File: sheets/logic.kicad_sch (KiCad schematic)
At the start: 25 parts, among them J6 MicroFit3.0_1x2, J7 MoRex_MicroFit-3.0_4x1, SW1 SW_Omron_B3FS, U5 ESP32-S3-DevKitC, U6 NRF24L01_Breakout, U7 PCA9685PW, U8 TCA9545APWR, U9 BTT_TMC2209

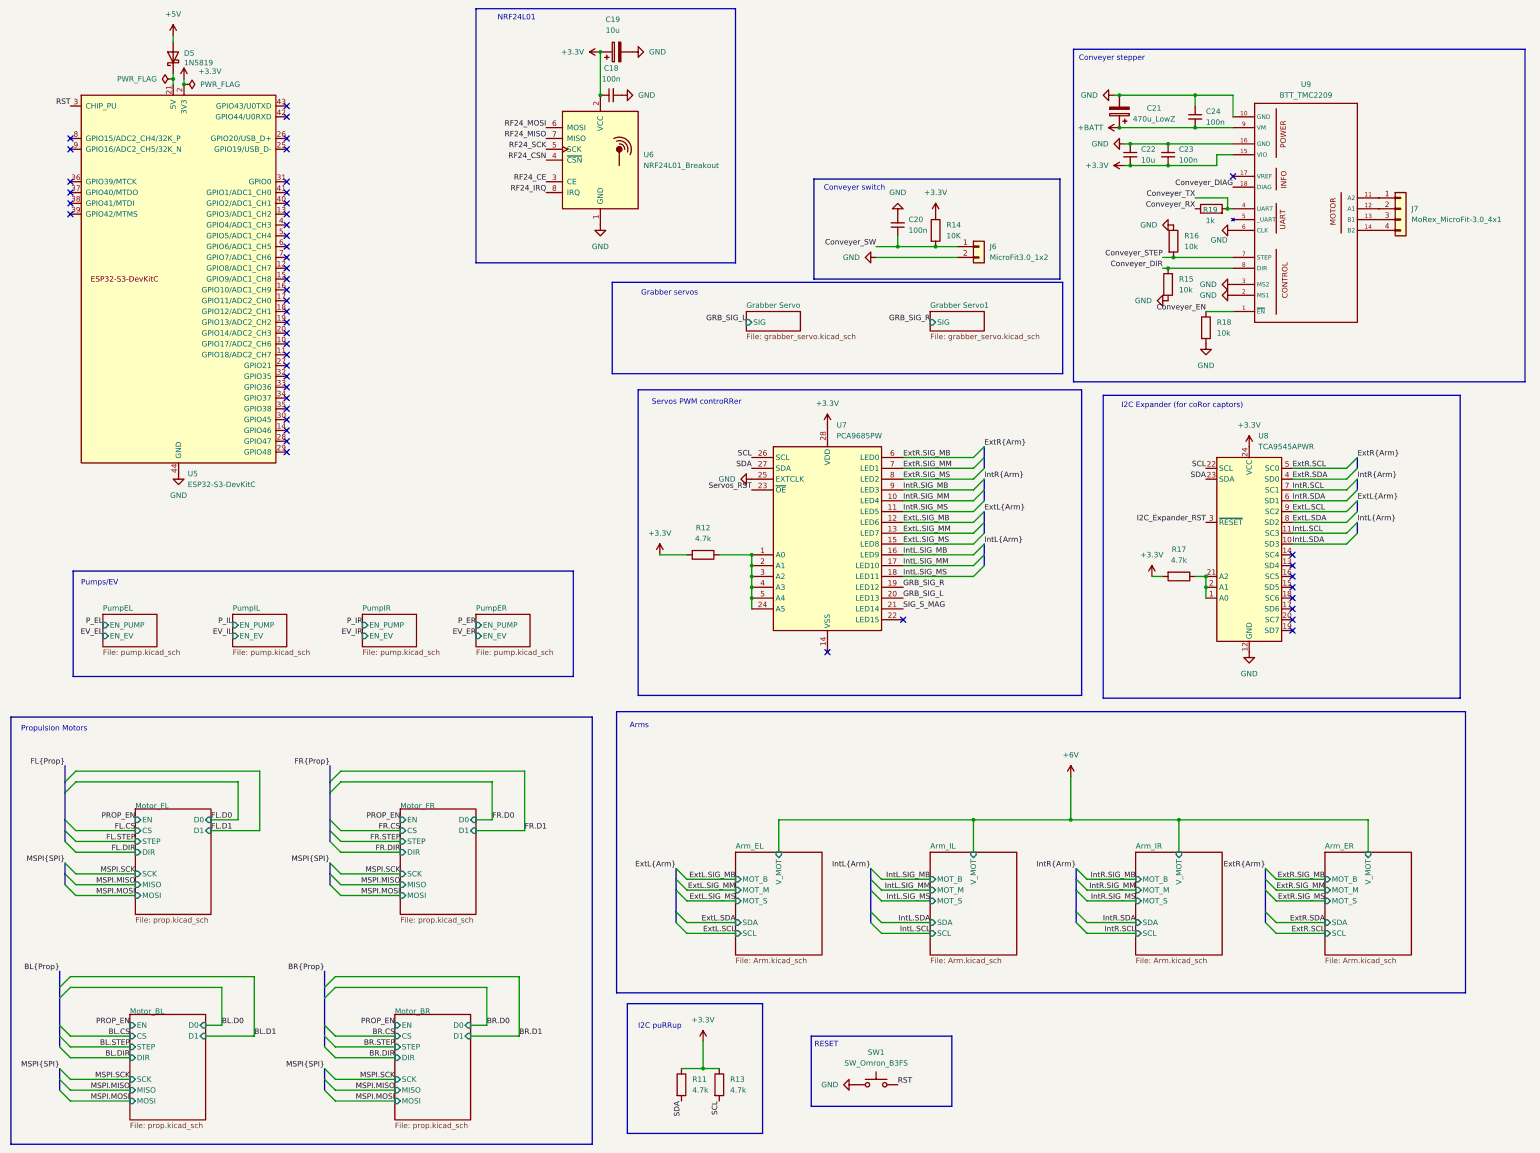
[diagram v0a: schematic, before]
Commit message: Add CB1-P-12V relay footprint, 3D model, and symbols
Added CB1-P-12V.stp 3D model and CB1P12V.kicad_mod footprint to the libs directory. Updated libs/sym.kicad_sym and multiple schematic sheets to include and reference the new relay. Adjusted eurobot-2026-robot-pcb.kicad_pro BOM and group settings to support new components.
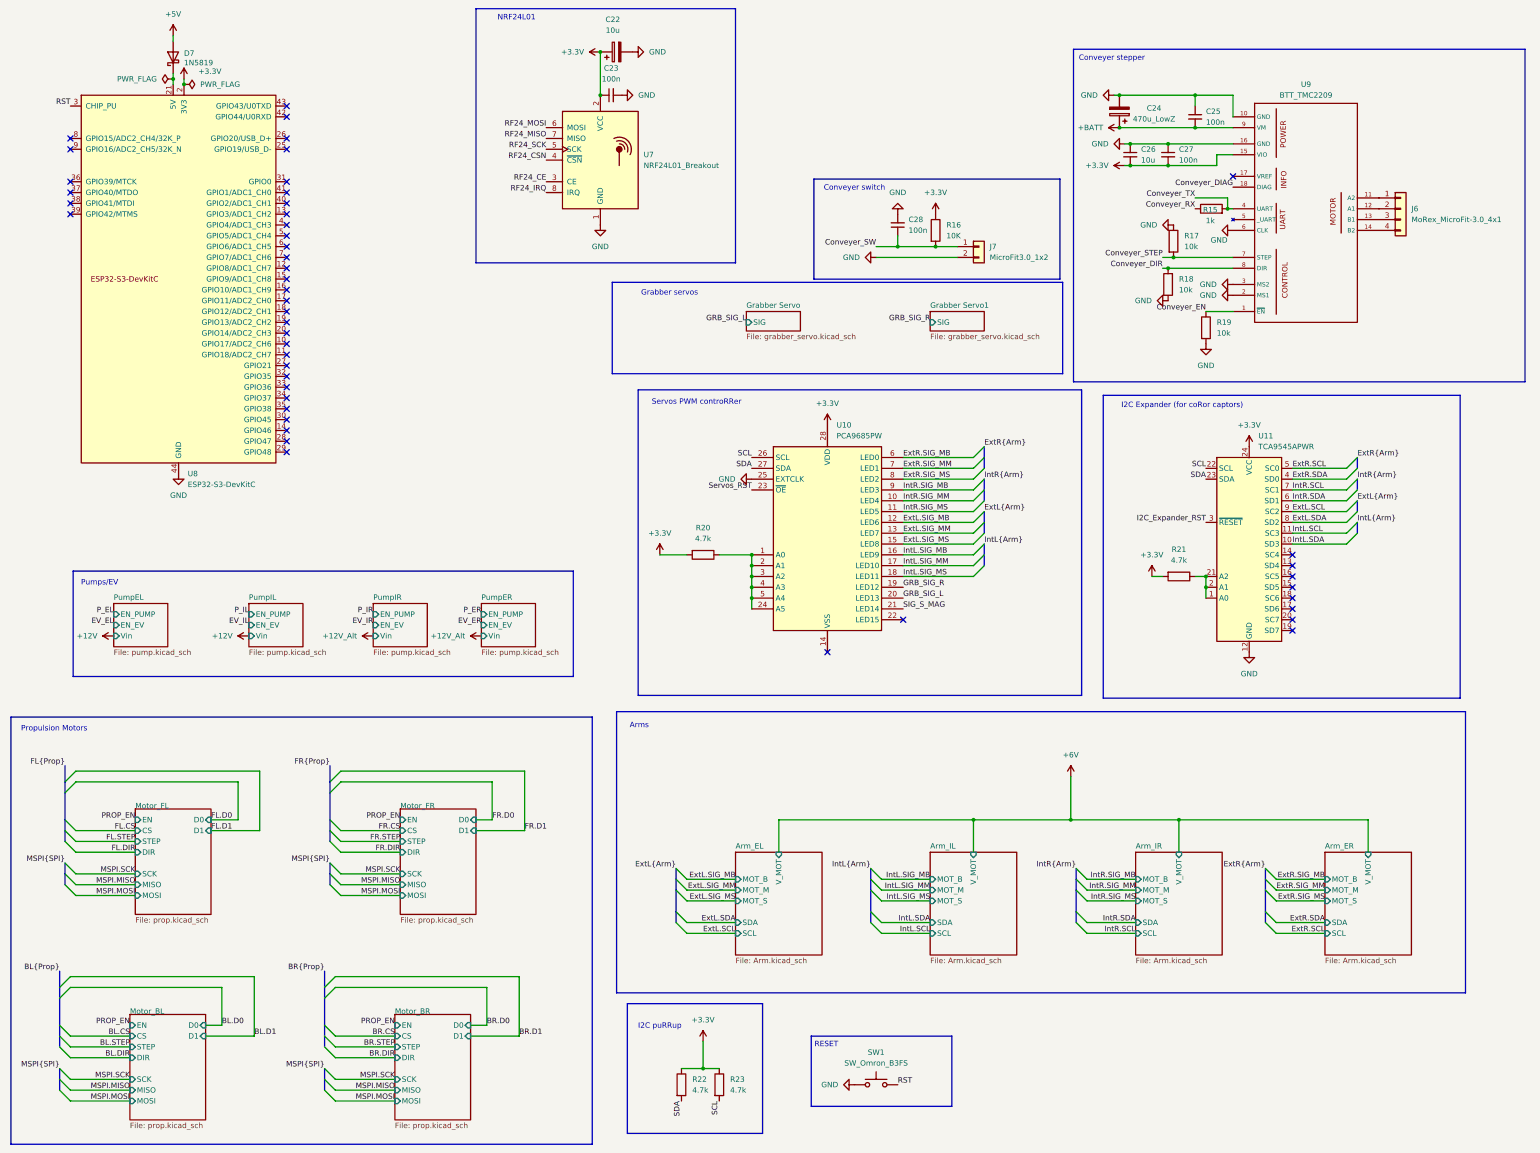
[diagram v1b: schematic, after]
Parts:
- renumbered C19 to C22, C18 to C23, C21 to C24, C24 to C25, C22 to C26, C23 to C27, C20 to C28, D5 to D7, J7 to J6, J6 to J7, R19 to R15, R14 to R16, R16 to R17, R15 to R18, R18 to R19, R12 to R20, R17 to R21, R11 to R22, R13 to R23, U7 to U10, U8 to U11, U6 to U7, U5 to U8
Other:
- sheet PumpEL ports: added Vin; removed none
- sheet PumpER ports: added Vin; removed none
- sheet PumpIL ports: added Vin; removed none
- sheet PumpIR ports: added Vin; removed none
